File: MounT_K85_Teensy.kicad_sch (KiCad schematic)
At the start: 9 parts, among them J1 Teensy_3.5_3.6_4.1_DIP_only, J2 DB25_Male, U1 MAX3232

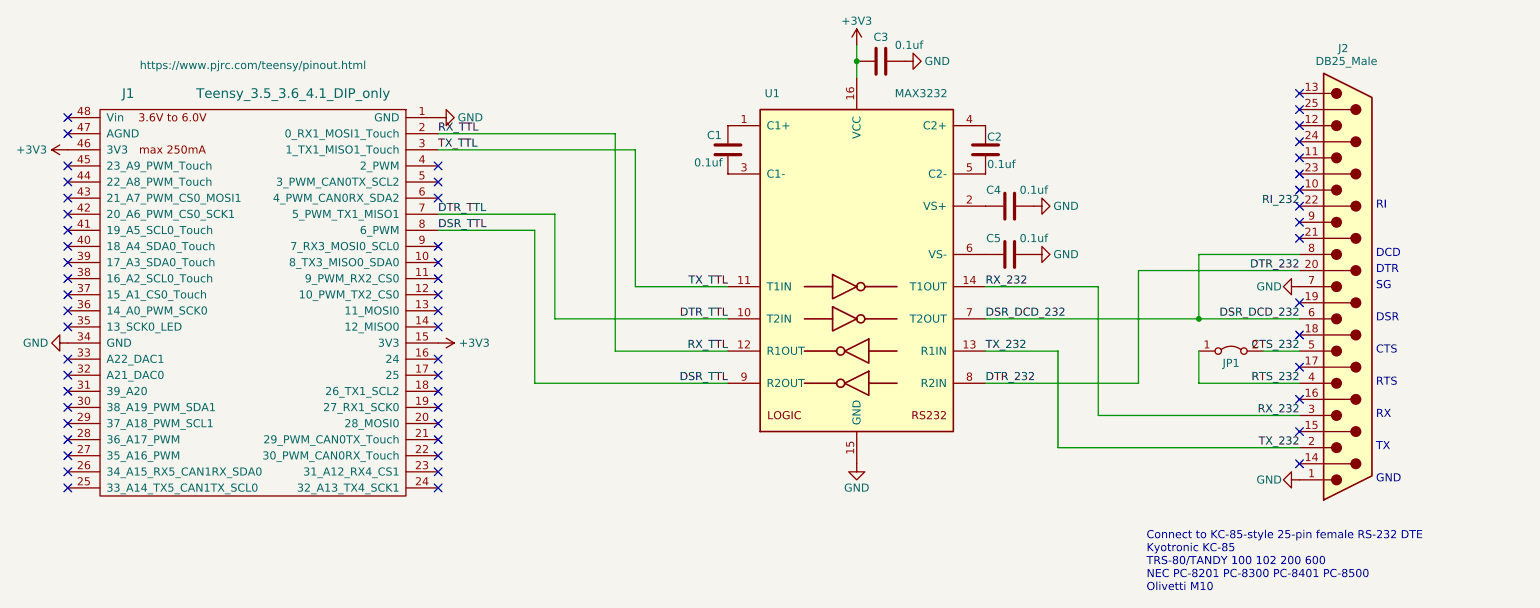
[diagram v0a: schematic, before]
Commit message: smt power switch on feather, routing 3v3 on teensy, silkscreen all
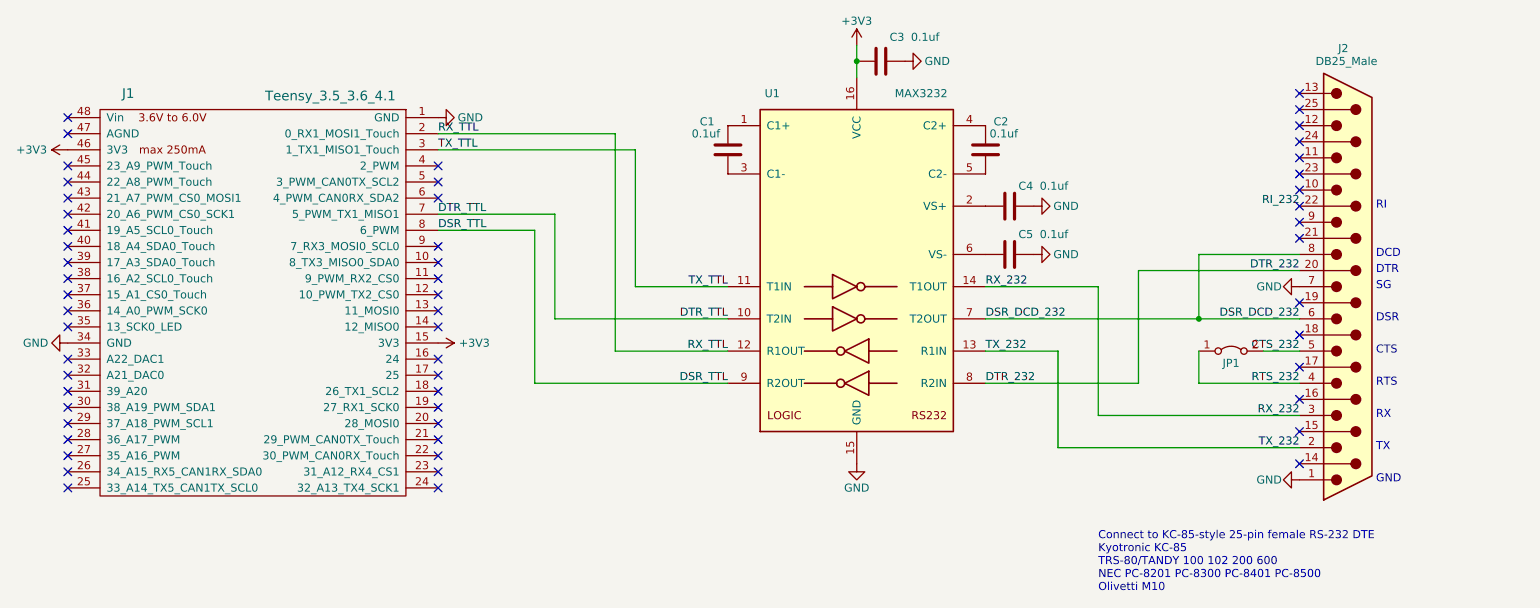
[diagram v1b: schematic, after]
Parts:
- J1: value Teensy_3.5_3.6_4.1_DIP_only -> Teensy_3.5_3.6_4.1; symbol 0_LOCAL:Teensy_3.5_3.6_4.1_DIP_only -> 0_LOCAL:Teensy_3.5_3.6_4.1; Pinouts https://www.pjrc.com/teensy/pinout.html -> (none)
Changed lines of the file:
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@@
   )
   (text "Connect to KC-85-style 25-pin female RS-232 DTE\nKyotronic KC-85\nTRS-80/TANDY 100 102 200 600\nNEC PC-8201 PC-8300 PC-8401 PC-8500\nOlivetti M10\n"
-    (at 204.47 152.4 0)
+    (at 196.85 152.4 0)
     (effects (font (size 1.27 1.27)) (justify left bottom))
   )
@@
   (symbol (lib_id "0_LOCAL:C") (at 179.07 82.55 0) (unit 1)
     (in_bom yes) (on_board yes)
-    (property "Reference" "C2" (id 0) (at 179.324 80.518 0)
+    (property "Reference" "C2" (id 0) (at 180.34 78.105 0)
       (effects (font (size 1.27 1.27)) (justify left))
     )
-    (property "Value" "0.1uf" (id 1) (at 179.324 84.836 0)
+    (property "Value" "0.1uf" (id 1) (at 179.705 80.01 0)
       (effects (font (size 1.27 1.27)) (justify left))
     )
@@
   (symbol (lib_id "0_LOCAL:C") (at 138.43 82.55 0) (unit 1)
     (in_bom yes) (on_board yes)
-    (property "Reference" "C1" (id 0) (at 135.128 80.264 0)
+    (property "Reference" "C1" (id 0) (at 133.985 78.105 0)
       (effects (font (size 1.27 1.27)) (justify left))
     )
-    (property "Value" "0.1uf" (id 1) (at 133.096 84.582 0)
+    (property "Value" "0.1uf" (id 1) (at 132.715 80.01 0)
       (effects (font (size 1.27 1.27)) (justify left))
     )
@@
   (symbol (lib_id "0_LOCAL:C") (at 182.88 91.44 90) (unit 1)
     (in_bom yes) (on_board yes)
-    (property "Reference" "C4" (id 0) (at 180.34 88.9 90))
-    (property "Value" "0.1uf" (id 1) (at 186.69 88.9 90))
+    (property "Reference" "C4" (id 0) (at 185.42 88.265 90))
+    (property "Value" "0.1uf" (id 1) (at 189.865 88.265 90))
     (property "Footprint" "0_LOCAL:C_0805" (id 2) (at 186.69 90.4748 0)
       (effects (font (size 1.27 1.27)) hide)
@@
   (symbol (lib_id "0_LOCAL:C") (at 182.88 99.06 90) (unit 1)
     (in_bom yes) (on_board yes)
-    (property "Reference" "C5" (id 0) (at 180.34 96.52 90))
-    (property "Value" "0.1uf" (id 1) (at 186.69 96.52 90))
+    (property "Reference" "C5" (id 0) (at 185.42 95.885 90))
+    (property "Value" "0.1uf" (id 1) (at 189.865 95.885 90))
     (property "Footprint" "0_LOCAL:C_0805" (id 2) (at 186.69 98.0948 0)
       (effects (font (size 1.27 1.27)) hide)
@@
   (symbol (lib_id "0_LOCAL:C") (at 162.56 68.58 90) (unit 1)
     (in_bom yes) (on_board yes)
-    (property "Reference" "C3" (id 0) (at 162.56 64.77 90))
-    (property "Value" "0.1uf" (id 1) (at 167.005 66.04 90))
+    (property "Reference" "C3" (id 0) (at 165.1 64.77 90))
+    (property "Value" "0.1uf" (id 1) (at 169.545 64.77 90))
     (property "Footprint" "0_LOCAL:C_0805" (id 2) (at 166.37 67.6148 0)
       (effects (font (size 1.27 1.27)) hide)
@@
     (pin "1")
   )
-  (symbol (lib_id "0_LOCAL:Teensy_3.5_3.6_4.1_DIP_only") (at 63.5 106.68 0) (mirror y) (unit 1)
+  (symbol (lib_id "0_LOCAL:Teensy_3.5_3.6_4.1") (at 63.5 106.68 0) (mirror y) (unit 1)
     (in_bom yes) (on_board yes)
     (property "Reference" "J1" (id 0) (at 43.815 73.66 0)
       (effects (font (size 1.524 1.524)))
     )
-    (property "Value" "Teensy_3.5_3.6_4.1_DIP_only" (id 1) (at 69.85 73.66 0)
-      (effects (font (size 1.524 1.524)))
-    )
-    (property "Footprint" "0_LOCAL:Teensy_3.5_3.6_4.1_DIP_friction" (id 2) (at 63.5 60.96 0)
+    (property "Value" "Teensy_3.5_3.6_4.1" (id 1) (at 65.405 74.93 0)
+      (effects (font (size 1.524 1.524)) (justify right bottom))
+    )
+    (property "Footprint" "0_LOCAL:Teensy_3.5_3.6_4.1_DIP_friction" (id 2) (at 63.5 139.7 0)
       (effects (font (size 1.524 1.524)) hide)
     )
-    (property "Datasheet" "https://www.pjrc.com/teensy/card8a_rev2.pdf" (id 3) (at 63.5 62.23 0)
+    (property "Datasheet" "https://www.pjrc.com/teensy/pinout.html" (id 3) (at 63.5 143.51 0)
       (effects (font (size 1.524 1.524)) hide)
     )
-    (property "Pinouts" "https://www.pjrc.com/teensy/pinout.html" (id 4) (at 63.5 69.215 0))
     (pin "1")
     (pin "10")
@@
     )
     (path "/5a4b72c7-7618-4b66-a2ee-c09368d229fc"
-      (reference "J1") (unit 1) (value "Teensy_3.5_3.6_4.1_DIP_only") (footprint "0_LOCAL:Teensy_3.5_3.6_4.1_DIP_friction")
+      (reference "J1") (unit 1) (value "Teensy_3.5_3.6_4.1") (footprint "0_LOCAL:Teensy_3.5_3.6_4.1_DIP_friction")
     )
     (path "/00000000-0000-0000-0000-00005f04b532"
